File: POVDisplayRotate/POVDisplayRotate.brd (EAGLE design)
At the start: 52 x 86 mm, 48 parts, among them U1 STP08DP05, U2 STP08DP05, U3 MPQ4420Q, U5 CY8CKIT-142, U6 M95M01

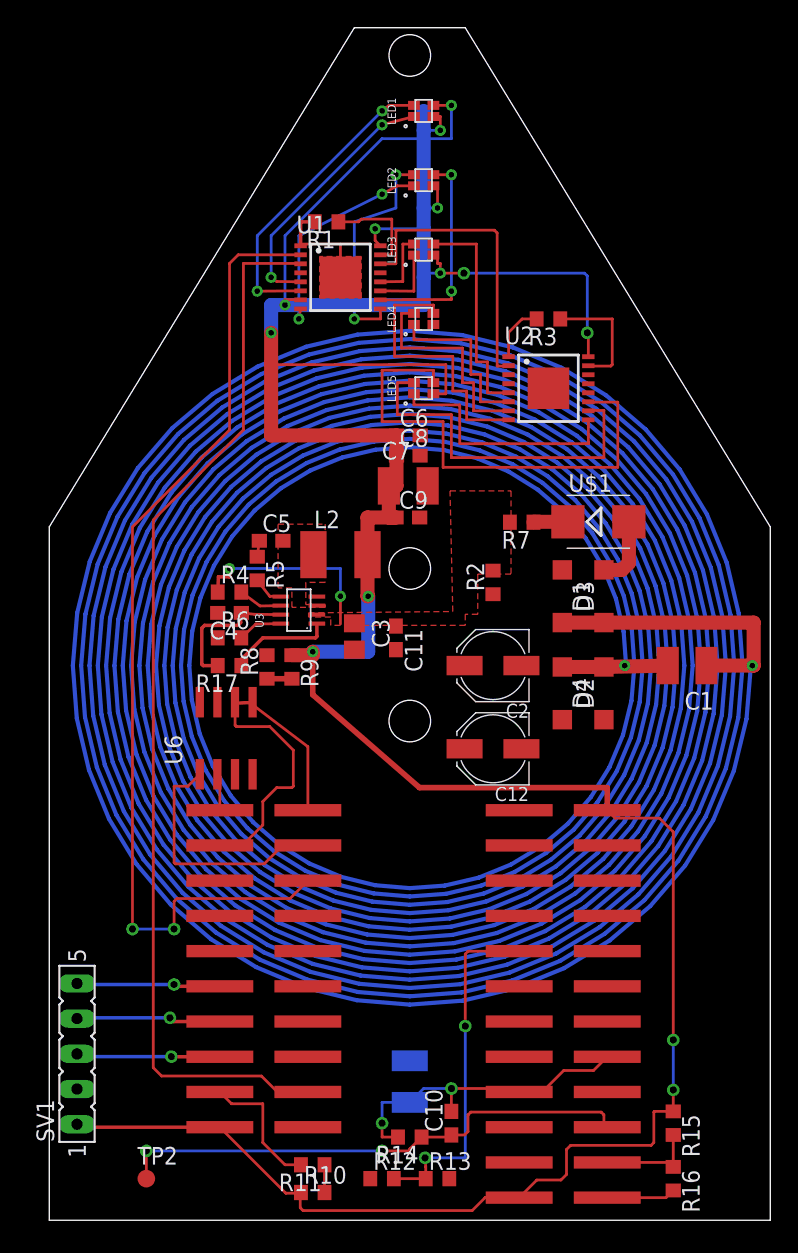
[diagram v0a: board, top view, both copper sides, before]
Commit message: Completed the routing of the POV Rotate board
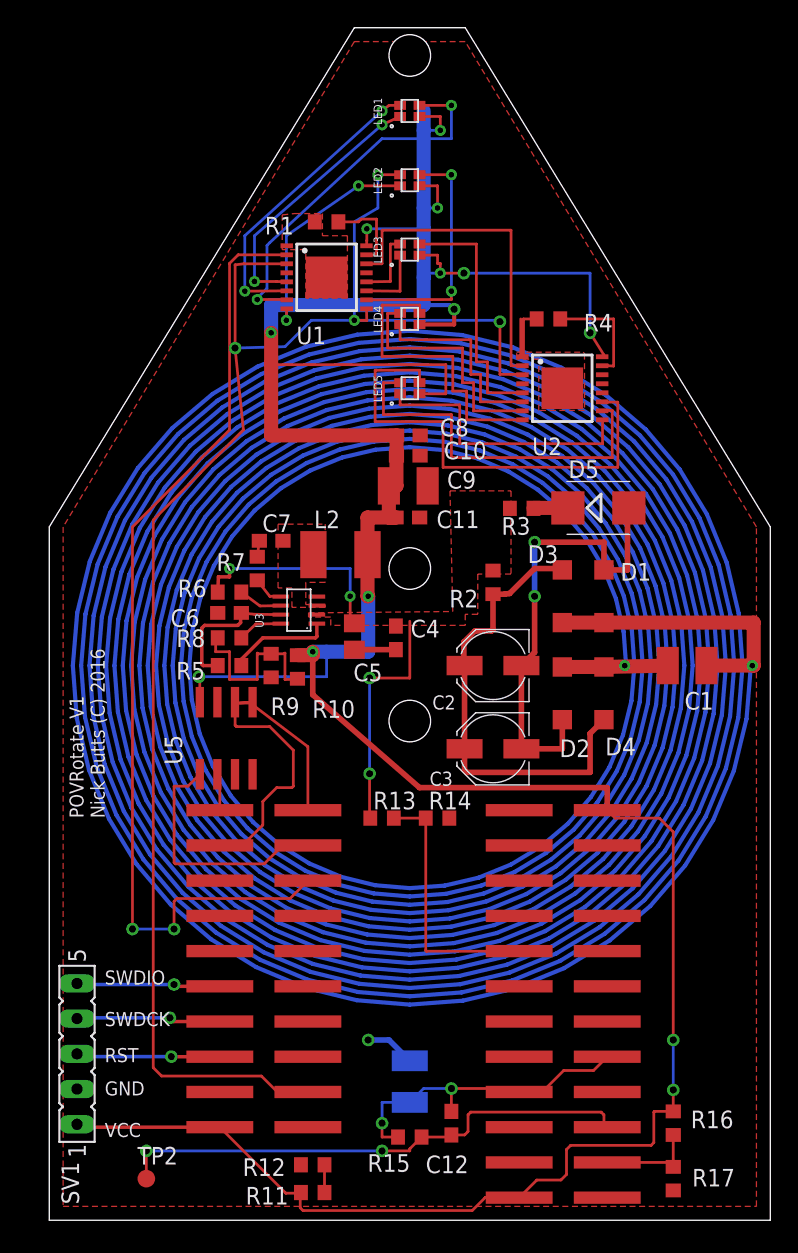
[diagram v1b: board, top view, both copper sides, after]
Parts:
- removed U$1: TVS, NicksParts:SMB
- removed U6: M95M01, NicksParts:SO-08
- added D5: TVS, NicksParts:SMB
- added U4: CY8CKIT-142, NicksParts:CY8CKIT-142
- C10: value 5p -> 10u
- C11: value 0.1u -> 1u
- C12: value 22u -> 5p; device resistor:PANASONIC_C -> resistor:C0603
- C3: device resistor:C0805 -> resistor:PANASONIC_C
- C5: value 100n -> 22u; device resistor:C0603 -> resistor:C0805
- C6: value 47u -> 0.1u
- C7: value 100u -> 100n; device resistor:C1210 -> resistor:C0603
- C8: value 10u -> 47u
- C9: value 1u -> 100u; device resistor:C0603 -> resistor:C1210
- R10: value 12k -> 41.2k
- R12: value 820k -> 12k
- R13: value 33k -> 820k
- R14: value 100k -> 33k
- R15: value 12k -> 100k
- R16: value 3k -> 12k
- R17: value 100k -> 3k
- R3: value 386 -> 120
- R4: value 1M -> 386
- R5: value 20 -> 100k
- R6: value 51k -> 1M
- R7: value 120 -> 20
- R8: value 7.68k -> 51k
- R9: value 41.2k -> 7.68k
- U5: value CY8CKIT-142 -> M95M01; device NicksParts:CY8CKIT-142 -> NicksParts:SO-08
- moved R17 48.9 mm to (45.0, 3.00), turned to 270 degrees
- moved C10 48.2 mm to (25.9, 55.1), turned to 0 degrees
- moved R10 37.9 mm to (17.9, 39.9), turned to 270 degrees
- moved R4 30.3 mm to (36.0, 65.0), turned to 180 degrees
- moved C12 27.2 mm to (29.0, 7.00), turned to 90 degrees
- moved R13 26.3 mm to (24.0, 29.0)
- moved R14 23.1 mm to (28.0, 29.0), turned to 0 degrees
- moved U5 21.4 mm to (12.8, 34.8)
- moved R7 19.4 mm to (15.0, 47.0), turned to 270 degrees
- moved R15 19.0 mm to (26.0, 6.00), turned to 180 degrees
- moved C6 18.2 mm to (13.0, 43.8), turned to 180 degrees
- moved R3 13.8 mm to (34.1, 51.3)
- moved C3 12.9 mm to (32.0, 34.0), turned to 180 degrees
- moved C4 12.1 mm to (25.0, 42.0), turned to 270 degrees
- moved C7 10.7 mm to (16.0, 49.0)
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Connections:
- removed net AGND: C11.2, C12.-, C2.-, C3.2, C4.2, C6.2, C7.2, C8.2, C9.2, D1.A, D2.A, D6.P$1, R1.2, R11.2, R13.2, R16.2, R3.2, R8.2, U$1.A, U1.1, U1.GND, U2.1, U2.GND, U3.4, U5.GND, U5.GND1, U5.GND2
- new net N$17: C2.-, C3.-, D1.A, D2.A, D5.A
- net DAC_OUT: now also R16.2, R17.1, U4.2.1; no longer R15.2, R16.1, U5.2.1
- net EE_CS: now also U4.0.2, U5.1; no longer U5.0.2, U6.1
- net EE_HOLD: now also U5.7; no longer U6.7
- net EE_MISO: now also U4.0.1, U5.2; no longer U5.0.1, U6.2
- net EE_MOSI: now also U4.0.0, U5.5; no longer U5.0.0, U6.5
- net EE_SCLK: now also U4.0.3, U5.6; no longer U5.0.3, U6.6
- net EE_WP: now also U5.3; no longer U6.3
- net GND: now also C10.2, C11.2, C4.2, C5.2, C6.2, C8.2, C9.2, D6.P$1, R1.2, R12.2, R14.2, R17.2, R4.2, R9.2, U1.1, U1.GND, U2.1, U2.GND, U3.4, U4.GND, U4.GND1, U4.GND2, U5.4; no longer U6.4
- net IN_PWR: now also R13.2, R14.1, U4.3.0; no longer R12.2, R13.1, U5.3.0
- net N$1: now also C6.1, R5.2; no longer C4.1, R17.2
- net N$10: now also R4.1; no longer R3.1
- net N$11: now also D5.C, R3.1; no longer R7.1, U$1.C
- net N$13: now also R5.1; no longer R17.1
- net N$2: now also R6.2; no longer R4.2
- net N$3: now also C3.+; no longer C12.+
- net N$4: now also R8.2; no longer R6.2
- net N$5: now also R10.2, R9.1; no longer R6.1, R9.2
- net N$7: now also R7.2; no longer R5.2
- net N$8: now also C7.1, R7.1; no longer C5.1, R5.1
- net OPAMP1_NEG: now also C12.2, R15.2, U4.2.4, U4.2.7; no longer C10.2, R14.2, U5.2.4, U5.2.7
- net OPAMP1_OUT: now also C12.1, R15.1, U4.2.3; no longer C10.1, R14.1, U5.2.3
- net OPAMP1_PLUS: now also R11.2, R12.1; no longer R10.2, R11.1
- net SCLK: now also U4.1.7; no longer U5.1.7
- net SDI: now also U4.0.4; no longer U5.0.4
- net SWDCLK: now also U4.0.7; no longer U5.0.7
- net SWDIO: now also U4.0.6; no longer U5.0.6
- net SWOUT: now also C7.2; no longer C5.2
- net V+: now also C4.1, C5.1, R13.1, R3.2, R6.1; no longer C11.1, C3.1, R12.1, R4.1, R7.2
- net VCC: now also C10.1, C11.1, R11.1, R16.1, U4.VDDA, U4.VDDD, U4.VDDR, U5.8; no longer C6.1, C7.1, R15.1, R9.1, U5.VDDA, U5.VDDD, U5.VDDR, U6.8
- net XRES: now also U4.XRES; no longer U5.XRES
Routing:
- net N$17: track 0.00 -> 33.6 mm, vias 0 -> 2
- net N$3: track 0.00 -> 33.4 mm
- net AGND: track 31.8 -> 0.00 mm
- net SCLK: track 76.7 -> 101.7 mm, vias 0 -> 2
- net VCC: track 219.7 -> 243.3 mm, vias 11 -> 13
- net V+: track 14.5 -> 32.3 mm, vias 2 -> 4
- net GND: track 0.00 -> 13.1 mm, vias 0 -> 1
- net N$5: track 1.80 -> 12.8 mm
- net IN_PWR: track 25.4 -> 18.6 mm, vias 2 -> 0
- net BLED1: track 25.1 -> 27.3 mm
- net N$18: track 21.4 -> 23.4 mm
- net RLED4: track 12.4 -> 14.4 mm
- net GLED4: track 15.7 -> 17.7 mm
- net BLED3: track 16.2 -> 18.2 mm
- net BLED2: track 15.4 -> 17.4 mm
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- added copper zone on layer 1, net GND
- removed copper zone on layer 1, net N$9
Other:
- board text added: "GND"
- board text added: "POVRotate V1 Nick Butts (C) 2016"
- board text added: "RST"
- board text added: "SWDCK"
- board text added: "SWDIO"
- board text added: "VCC"

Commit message: Moved EEP to get more room
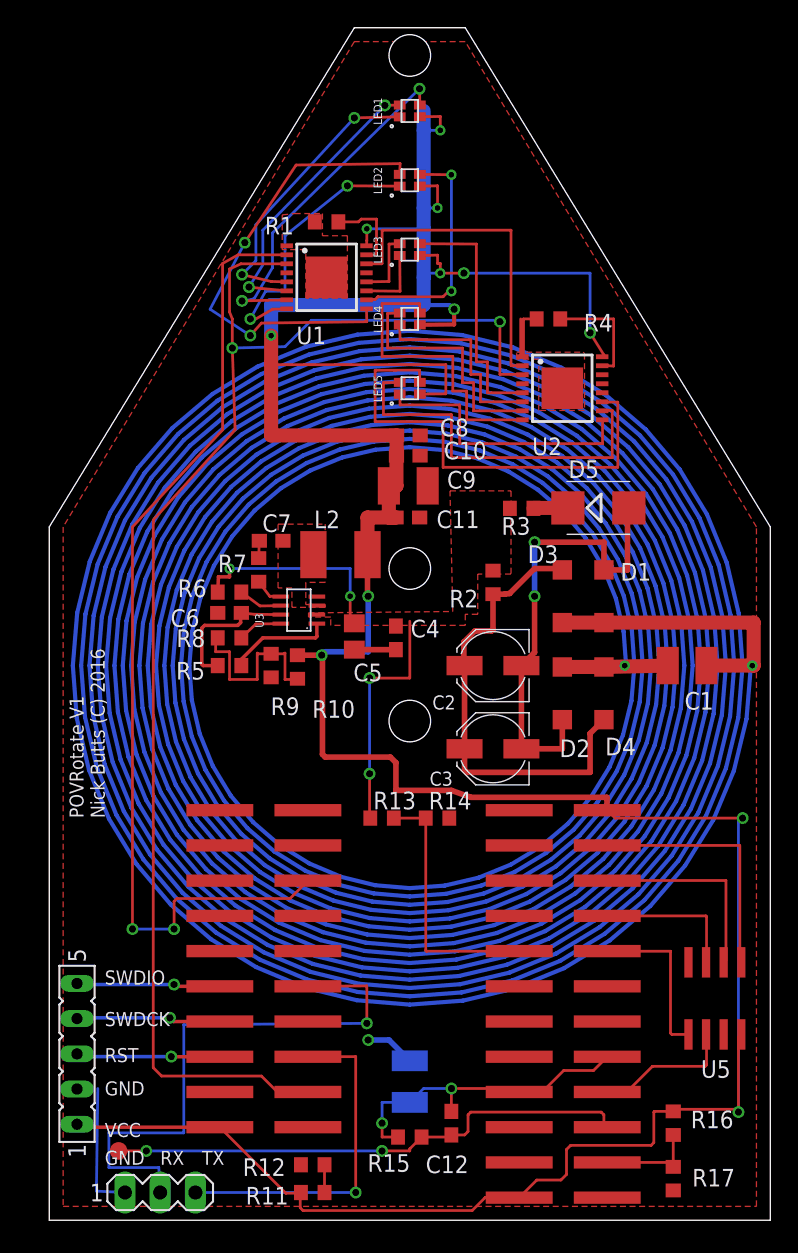
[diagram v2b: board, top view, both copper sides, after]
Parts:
- added SV2: (no value), con-lstb:MA03-1
- moved U5 39.9 mm to (48.0, 16.0), turned to 180 degrees
- moved TP2 2.83 mm to (5.00, 5.00)
- moved R7 0.14 mm to (15.1, 46.9)
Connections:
- new net HOLD: U4.5.0
- new net RX: SV2.2, U4.1.4
- new net TX: SV2.3, U4.1.5
- net EE_CS: now also U4.3.7; no longer U4.0.2
- net EE_MISO: now also U4.3.5; no longer U4.0.1
- net EE_MOSI: now also U4.3.1; no longer U4.0.0
- net EE_SCLK: now also U4.2.5; no longer U4.0.3
- net EE_WP: now also U4.3.3
- net GND: now also SV2.1
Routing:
- net RX: track 0.00 -> 41.3 mm, vias 0 -> 1
- net TX: track 0.00 -> 24.8 mm, vias 0 -> 1
- net GLED2: track 14.8 -> 33.6 mm
- net EE_MISO: track 2.66 -> 14.5 mm
- net EE_WP: track 0.00 -> 10.5 mm
- net GND: track 13.1 -> 22.6 mm
- net EE_SCLK: track 17.3 -> 10.2 mm
- net VCC: track 243.3 -> 248.6 mm, vias 13 -> 12
- net RLED2: track 16.2 -> 20.0 mm
- net BLED1: track 27.3 -> 25.2 mm
- net RLED1: track 19.2 -> 21.0 mm
- net GLED1: track 21.8 -> 20.8 mm
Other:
- board text added: "RX"
- board text added: "TX"
